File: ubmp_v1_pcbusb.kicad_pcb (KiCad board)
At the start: 2 copper layers, 40.1 x 14 mm, 34 parts, among them J1 Conn_02x05_Counter_Clockwise, J2 USB_A, U1 STM32F103CBUx, U2 MIC5245-3.3, Y1 PRQC8.00CR1010V00L

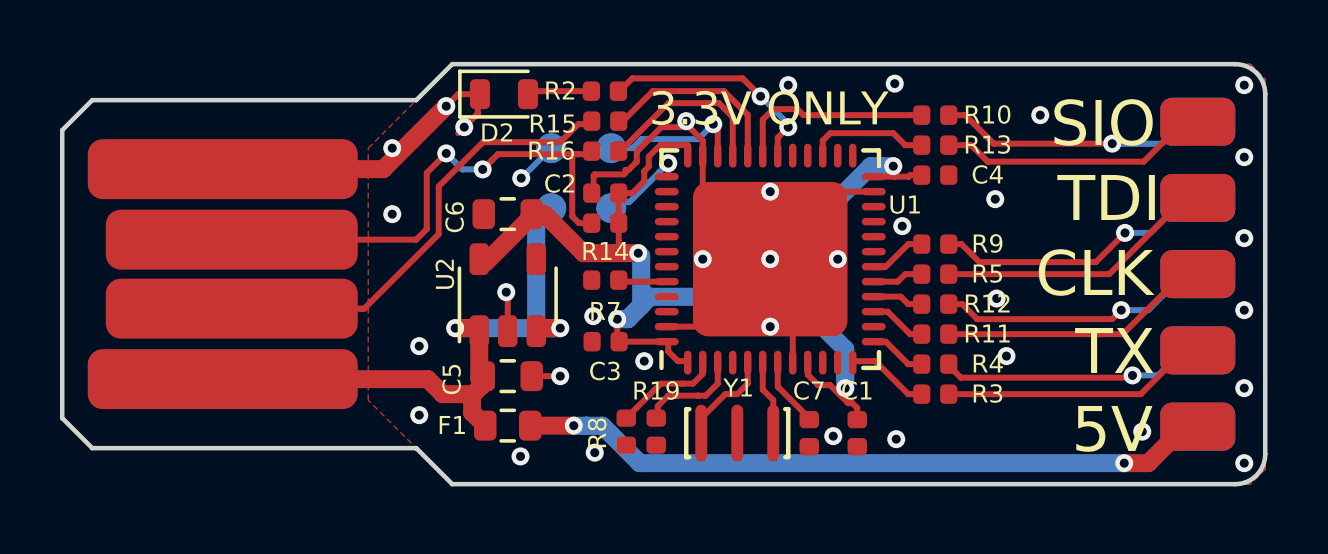
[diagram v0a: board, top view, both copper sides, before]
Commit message: Changed all 100 and 22 ohm resistors to ESD chips with built in resistors
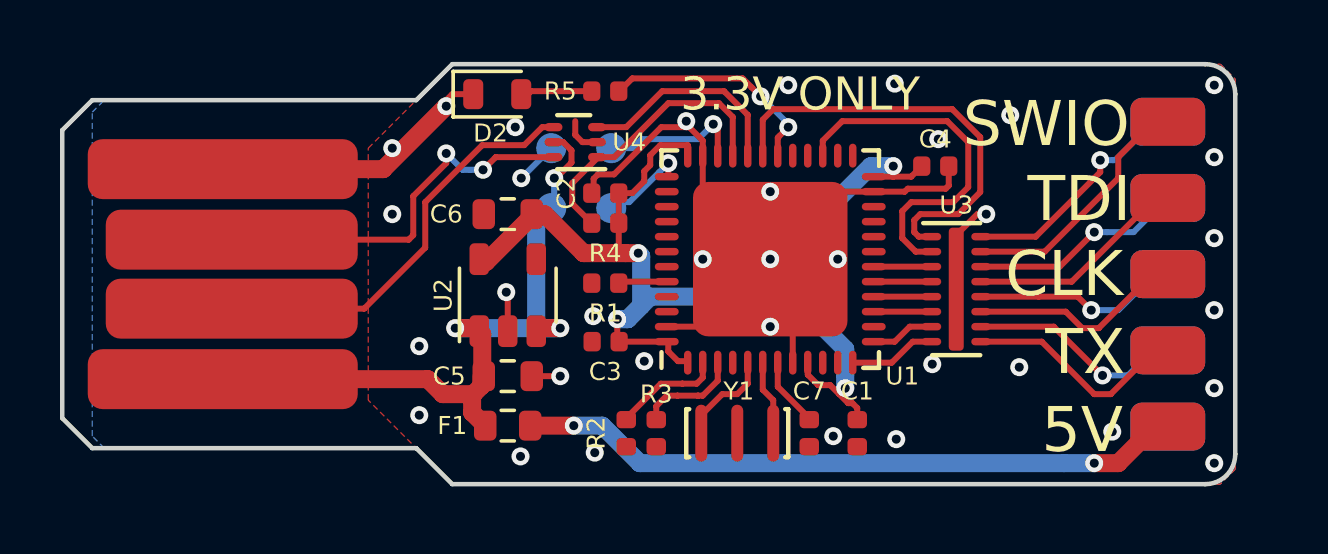
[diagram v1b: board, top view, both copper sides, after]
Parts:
- removed R10, R11, R12, R13: 100, ubmp:R_0402_1005Metric_Rounded
- removed R14, R19, R7, R8: 1.5k, ubmp:R_0402_1005Metric_Rounded
- removed R15, R16, R9: 22, ubmp:R_0402_1005Metric_Rounded
- added R1: 1.5k, ubmp:R_0402_1005Metric_Rounded, F.Cu at (97.5, 106.3)
- added U3: NUF8401MNT4G, ubmp:DFN-16-1EP_1.6x4mm_P0.5mm, F.Cu at (109.2, 106.5)
- added U4: NUF2042XV6T1G, ubmp:DFN-6-1EP_1.2x1.6mm_P0.5mm, F.Cu at (96.5, 101.6)
- R2: value 470 -> 1.5k
- R3, R4: value 100 -> 1.5k
- R5: value 100 -> 470
- moved R5 12.6 mm to (97.5, 99.9)
- moved R4 12.0 mm to (97.5, 104.3)
- moved R2 11.4 mm to (98.2, 111.3), turned to 270 degrees
- moved R3 9.39 mm to (99.2, 111.3), turned to 270 degrees
- moved J1 1.00 mm to (116.2, 106.0)
- moved C4 0.30 mm to (108.5, 102.4)
- moved D2 0.22 mm to (93.9, 100.0)
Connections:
- R2 pad 1: /LED_STLINK -> /STM_ID
- R2 pad 2: Net-(D2-Pad2) -> GND
- R3 pad 1: /BMP_TXo -> /STM_ID2
- R3 pad 2: /BMP_TX -> GND
- R4 pad 1: /BMP_RXo -> +3V3
- R4 pad 2: /BMP_RX -> /DP_P
- R5 pad 1: /BMP_TDIo -> /LED_STLINK
- R5 pad 2: /BMP_TDI -> Net-(D2-Pad2)
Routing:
- net /BMP_SWDIO_TMS: track 4.12 -> 12.1 mm
- net /BMP_SWO: track 6.78 -> 14.5 mm
- net GND: track 37.9 -> 43.5 mm
- net /DP: track 17.9 -> 13.3 mm
- net /DP_P: track 6.05 -> 9.57 mm
- net +5V: track 21.9 -> 24.6 mm, vias 2 -> 3
- net /BMP_RSTo: track 9.50 -> 7.17 mm
- net /BMP_TDOo: track 9.19 -> 6.91 mm
- net /BMP_TDIo: track 9.41 -> 7.38 mm
- net /BMP_SWCLK_TCKo: track 9.19 -> 7.20 mm
- net /BMP_RXo: track 8.93 -> 7.24 mm
- net /DM: track 15.5 -> 14.1 mm
- net /BMP_TXo: track 8.97 -> 7.55 mm
- net Net-(F1-Pad1): track 23.3 -> 22.3 mm
- net /BMP_SWOo: track 9.00 -> 8.05 mm
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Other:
- board size 40.1 x 14 mm -> 39.1 x 14 mm
- board text added: "SWIO"
- board text added: "µBMP v1.2"
- board text removed: "SIO"
- board text removed: "µBMP v1.1"

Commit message: Split into hierarchical sheep
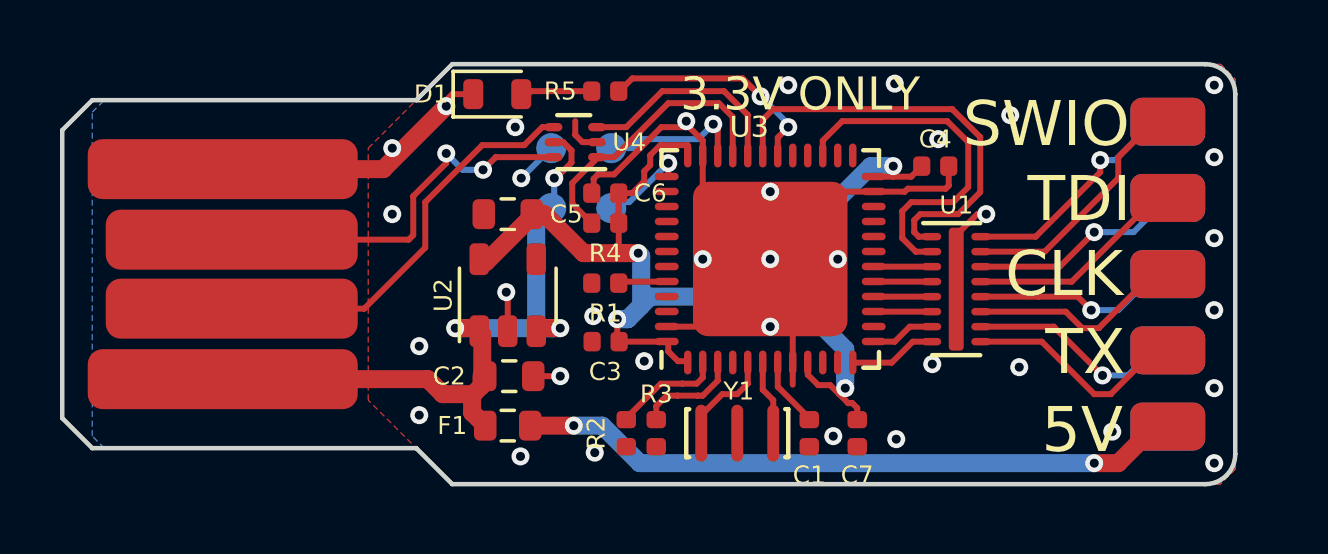
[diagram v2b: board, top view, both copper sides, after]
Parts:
- removed D2: GREEN, ubmp:D_0603_1608Metric_Rounded
- added D1: GREEN, ubmp:D_0603_1608Metric_Rounded, F.Cu at (93.9, 100.0)
- C2: value 100n -> 4.7u; footprint ubmp:C_0402_1005Metric_Rounded -> ubmp:C_0603_1608Metric_Rounded
- C6: value 4.7u -> 100n; footprint ubmp:C_0603_1608Metric_Rounded -> ubmp:C_0402_1005Metric_Rounded
- U1: value STM32F103CBUx -> NUF8401MNT4G; footprint ubmp:QFN-48-1EP_7x7mm_P0.5mm_EP5.15x5.15mm -> ubmp:DFN-16-1EP_1.6x4mm_P0.5mm
- U3: value NUF8401MNT4G -> STM32F103CBUx; footprint ubmp:DFN-16-1EP_1.6x4mm_P0.5mm -> ubmp:QFN-48-1EP_7x7mm_P0.5mm_EP5.15x5.15mm
- moved C2 6.89 mm to (94.3, 109.4), turned to 0 degrees
- moved U3 6.28 mm to (103.0, 105.5), turned to 90 degrees
- moved U1 6.28 mm to (109.2, 106.5), turned to 0 degrees
- moved C5 5.40 mm to (94.2, 104.0), turned to 180 degrees
- moved C6 3.32 mm to (97.5, 103.3)
- moved C1 1.60 mm to (104.3, 111.3), turned to 90 degrees
- moved C7 1.60 mm to (105.9, 111.3), turned to 270 degrees
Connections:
- C1 pad 1: +3V3 -> GND
- C1 pad 2: GND -> /bmp_core/NRST
- C2 pad 1: +3V3 -> +5V
- C5 pad 1: +5V -> +3V3
- C7 pad 1: GND -> +3V3
- C7 pad 2: /NRST -> GND
- J1 pad 2: /BMP_TXo -> /bmp_core/BMP_TXo
- J1 pad 3: /BMP_SWCLK_TCKo -> /bmp_core/BMP_SWCLK_TCKo
- J1 pad 4: /BMP_TDIo -> /bmp_core/BMP_TDIo
- J1 pad 5: /BMP_SWDIO_TMSo -> /bmp_core/BMP_SWDIO_TMSo
- J1 pad 6: /BMP_SWOo -> /bmp_core/BMP_SWOo
- J1 pad 7: /BMP_RSTo -> /bmp_core/BMP_RSTo
- J1 pad 8: /BMP_TDOo -> /bmp_core/BMP_TDOo
- J1 pad 9: /BMP_RXo -> /bmp_core/BMP_RXo
- R1 pad 1: /BOOT0 -> /bmp_core/BOOT0
- R2 pad 1: /STM_ID -> /bmp_core/STM_ID
- R3 pad 1: /STM_ID2 -> /bmp_core/STM_ID2
- R4 pad 2: /DP_P -> /bmp_core/DP_P
- R5 pad 1: /LED_STLINK -> /bmp_core/LED_STLINK
- TP1 pad 1: /SWDIO -> /bmp_core/SWDIO
- TP2 pad 1: /SWCLK -> /bmp_core/SWCLK
- U1 pad 1: +3V3 -> /bmp_core/BMP_SWO
- U1 pad 10: Net-(U1-Pad10) -> /bmp_core/BMP_RXo
- U1 pad 11: Net-(U1-Pad11) -> /bmp_core/BMP_SWCLK_TCKo
- U1 pad 12: /BMP_TX -> /bmp_core/BMP_TDOo
- U1 pad 13: /BMP_RX -> /bmp_core/BMP_TDIo
- U1 pad 14: Net-(U1-Pad14) -> /bmp_core/BMP_RSTo
- U1 pad 15: /BMP_SWCLK_TCK -> /bmp_core/BMP_SWDIO_TMSo
- U1 pad 16: /BMP_TDO -> /bmp_core/BMP_SWOo
- U1 pad 17: /BMP_TDI -> GND
- U1 pad 2: /STM_ID -> /bmp_core/BMP_SWDIO_TMS
- U1 pad 3: /STM_ID2 -> /bmp_core/BMP_RST
- U1 pad 4: Net-(U1-Pad4) -> /bmp_core/BMP_TDI
- U1 pad 5: Net-(U1-Pad5) -> /bmp_core/BMP_TDO
- U1 pad 6: Net-(U1-Pad6) -> /bmp_core/BMP_SWCLK_TCK
- U1 pad 7: /NRST -> /bmp_core/BMP_RX
- U1 pad 8: GND -> /bmp_core/BMP_TX
- U1 pad 9: +3V3 -> /bmp_core/BMP_TXo
- U3 pad 1: /BMP_SWO -> +3V3
- U3 pad 10: /BMP_RXo -> Net-(U3-Pad10)
- U3 pad 11: /BMP_SWCLK_TCKo -> Net-(U3-Pad11)
- U3 pad 12: /BMP_TDOo -> /bmp_core/BMP_TX
- U3 pad 13: /BMP_TDIo -> /bmp_core/BMP_RX
- U3 pad 14: /BMP_RSTo -> Net-(U3-Pad14)
- U3 pad 15: /BMP_SWDIO_TMSo -> /bmp_core/BMP_SWCLK_TCK
- U3 pad 16: /BMP_SWOo -> /bmp_core/BMP_TDO
- U3 pad 17: GND -> /bmp_core/BMP_TDI
- U3 pad 2: /BMP_SWDIO_TMS -> /bmp_core/STM_ID
- U3 pad 3: /BMP_RST -> /bmp_core/STM_ID2
- U3 pad 4: /BMP_TDI -> Net-(U3-Pad4)
- U3 pad 5: /BMP_TDO -> Net-(U3-Pad5)
- U3 pad 6: /BMP_SWCLK_TCK -> Net-(U3-Pad6)
- U3 pad 7: /BMP_RX -> /bmp_core/NRST
- U3 pad 8: /BMP_TX -> GND
- U3 pad 9: /BMP_TXo -> +3V3
- U4 pad 1: /DP_P -> /bmp_core/DP_P
- U4 pad 3: /DM_P -> /bmp_core/DM_P
- Y1 pad 1: Net-(U1-Pad5) -> Net-(U3-Pad5)
- Y1 pad 3: Net-(U1-Pad6) -> Net-(U3-Pad6)
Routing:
- net /bmp_core/BMP_SWO: track 0.00 -> 14.5 mm
- net /BMP_SWO: track 14.5 -> 0.00 mm
- net /bmp_core/BMP_SWDIO_TMS: track 0.00 -> 12.1 mm
- net /BMP_SWDIO_TMS: track 12.1 -> 0.00 mm
- net /bmp_core/DP_P: track 0.00 -> 9.57 mm
- net /DP_P: track 9.57 -> 0.00 mm
- net /bmp_core/BMP_SWDIO_TMSo: track 0.00 -> 8.43 mm
- net /BMP_SWDIO_TMSo: track 8.43 -> 0.00 mm
- net /bmp_core/BMP_SWOo: track 0.00 -> 8.05 mm, vias 0 -> 1
- net /BMP_SWOo: track 8.05 -> 0.00 mm, vias 1 -> 0
- net /bmp_core/LED_STLINK: track 0.00 -> 7.82 mm, vias 0 -> 2
- net /LED_STLINK: track 7.82 -> 0.00 mm, vias 2 -> 0
- net /bmp_core/BMP_TXo: track 0.00 -> 7.55 mm
- net /BMP_TXo: track 7.55 -> 0.00 mm
- net /bmp_core/BMP_TDIo: track 0.00 -> 7.38 mm
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
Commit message: Updated pinput
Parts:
- moved R4 0.10 mm to (97.5, 104.4)
- moved R3 0.10 mm to (99.3, 111.3)
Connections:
- J1 pad 4: /bmp_core/BMP_TDIo -> /bmp_core/BMP_RSTo
- J1 pad 7: /bmp_core/BMP_RSTo -> /bmp_core/BMP_TDIo
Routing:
- net GND: track 44.1 -> 40.9 mm, vias 35 -> 34
- net /DM: track 14.1 -> 13.5 mm
- net /DP: track 13.3 -> 12.8 mm
- net /bmp_core/BMP_RSTo: vias 1 -> 0
- net /bmp_core/BMP_TDIo: vias 0 -> 1
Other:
- board size 39.1 x 14 mm -> 38.9 x 14 mm

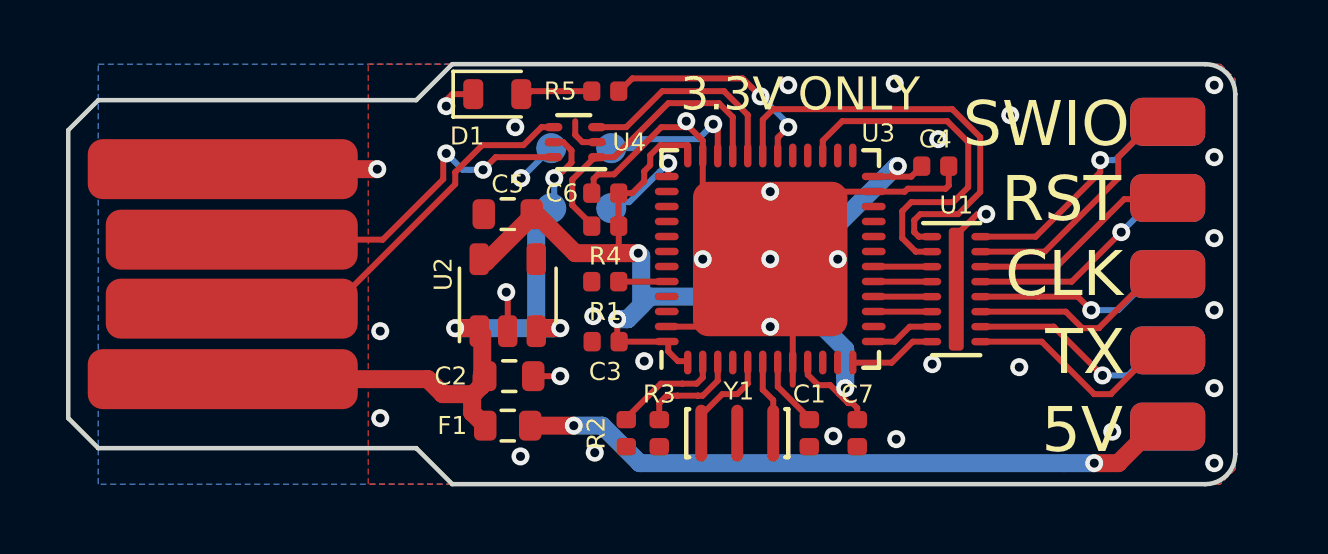
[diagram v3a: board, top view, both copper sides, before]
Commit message: Updated PCB USB version
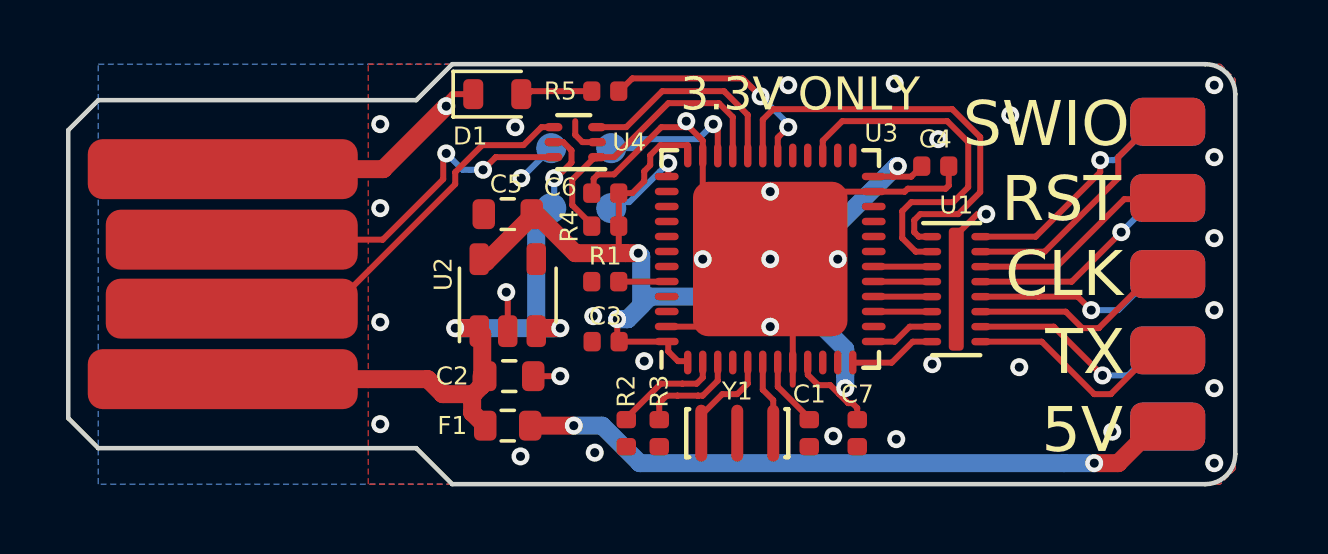
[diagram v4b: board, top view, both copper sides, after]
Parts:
- C1, C3, C4, C6, C7: footprint ubmp:C_0402_1005Metric_Rounded -> passive:C_0402_1005Metric_Rounded
- C2, C5: footprint ubmp:C_0603_1608Metric_Rounded -> passive:C_0603_1608Metric_Rounded
- D1: footprint ubmp:D_0603_1608Metric_Rounded -> passive:D_0603_1608Metric_Rounded
- F1: footprint ubmp:R_0603_1608Metric_Rounded -> passive:R_0603_1608Metric_Rounded
- J1: footprint ubmp:2x5_2.54mm_side -> connectors:2x5_2.54mm_side
- J2: footprint usbpcb:USBPCB -> usb:USBPCB
- R1, R2, R3, R4, R5: footprint ubmp:R_0402_1005Metric_Rounded -> passive:R_0402_1005Metric_Rounded
- U1: footprint ubmp:DFN-16-1EP_1.6x4mm_P0.5mm -> dfn:DFN-16-1EP_1.6x4mm_P0.5mm
- U2: footprint ubmp:SOT-23-5_Rounded -> sot:SOT-23-5
- U3: footprint ubmp:QFN-48-1EP_7x7mm_P0.5mm_EP5.15x5.15mm -> qfn:QFN-48-1EP_7x7mm_P0.5mm_EP5.15x5.15mm
- U4: footprint ubmp:DFN-6-1EP_1.2x1.6mm_P0.5mm -> dfn:DFN-6-1EP_1.2x1.6mm_P0.5mm
- Y1: footprint ubmp:Resonator_3pin_3.2x1.3mm -> crystals:Resonator_3pin_3.2x1.3mm
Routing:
- net GND: track 40.9 -> 44.1 mm, vias 34 -> 35
